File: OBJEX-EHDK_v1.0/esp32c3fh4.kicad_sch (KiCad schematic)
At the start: 34 parts

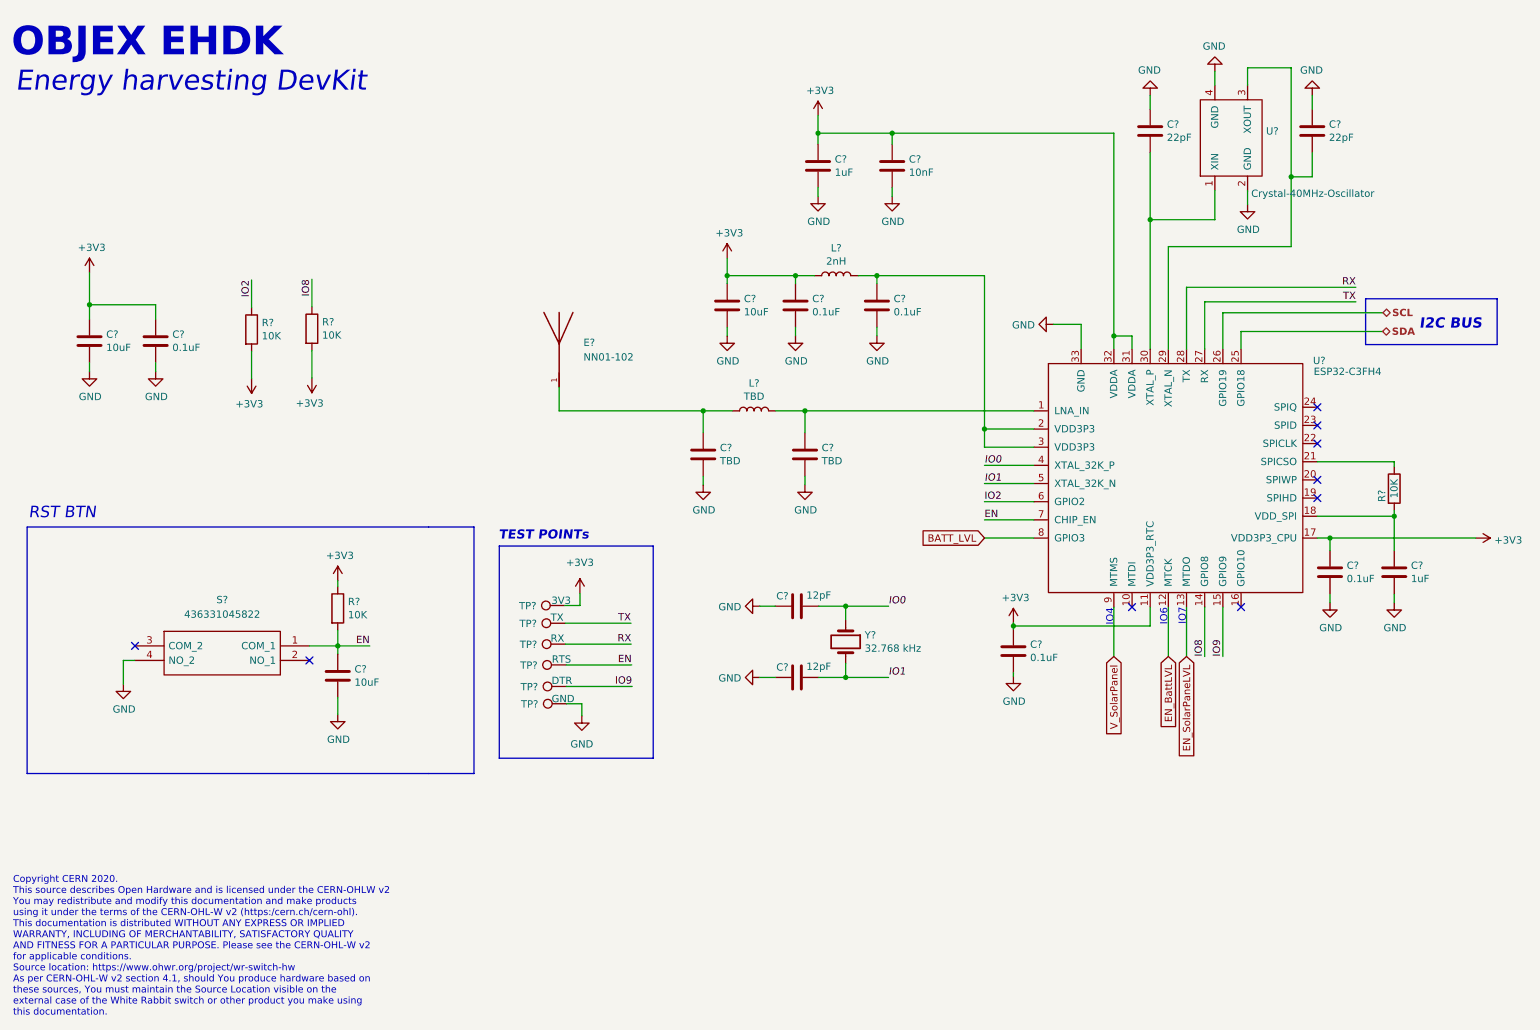
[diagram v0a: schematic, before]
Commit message: add: nRF52840 & SPV1050TTR
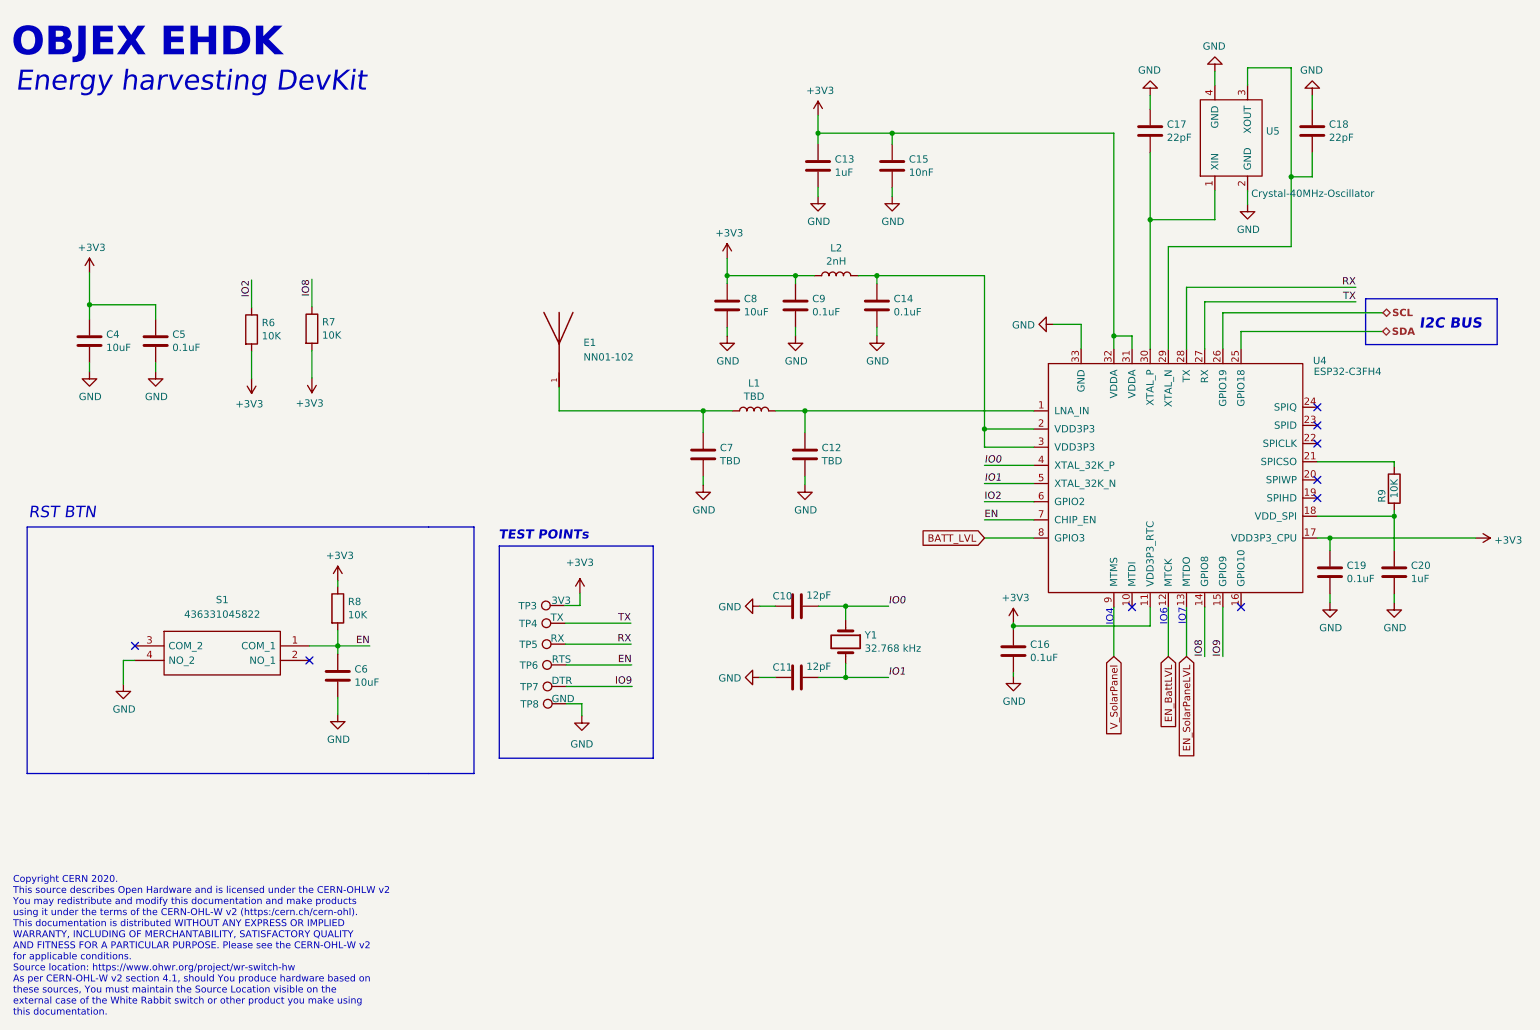
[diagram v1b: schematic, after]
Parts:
- gave numbers to parts that had none: 34

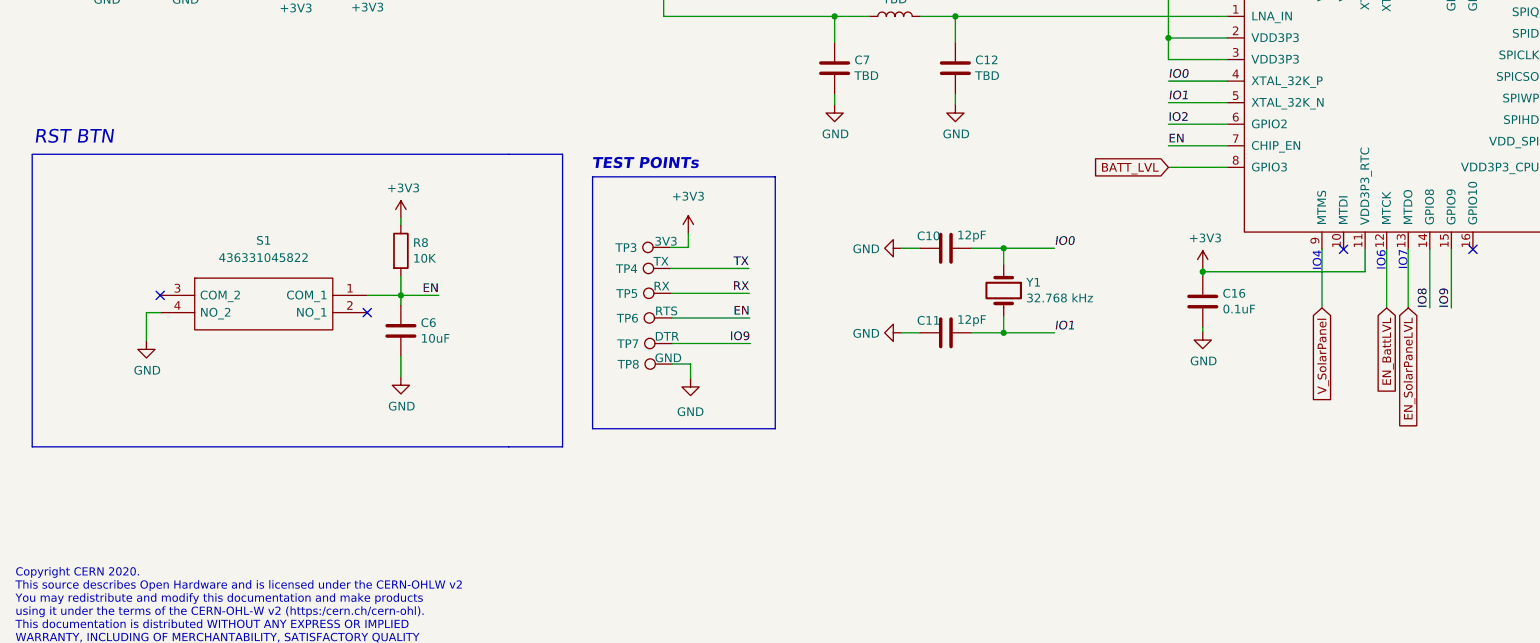
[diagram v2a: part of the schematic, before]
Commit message: Update design, EH ICs & Battery conn
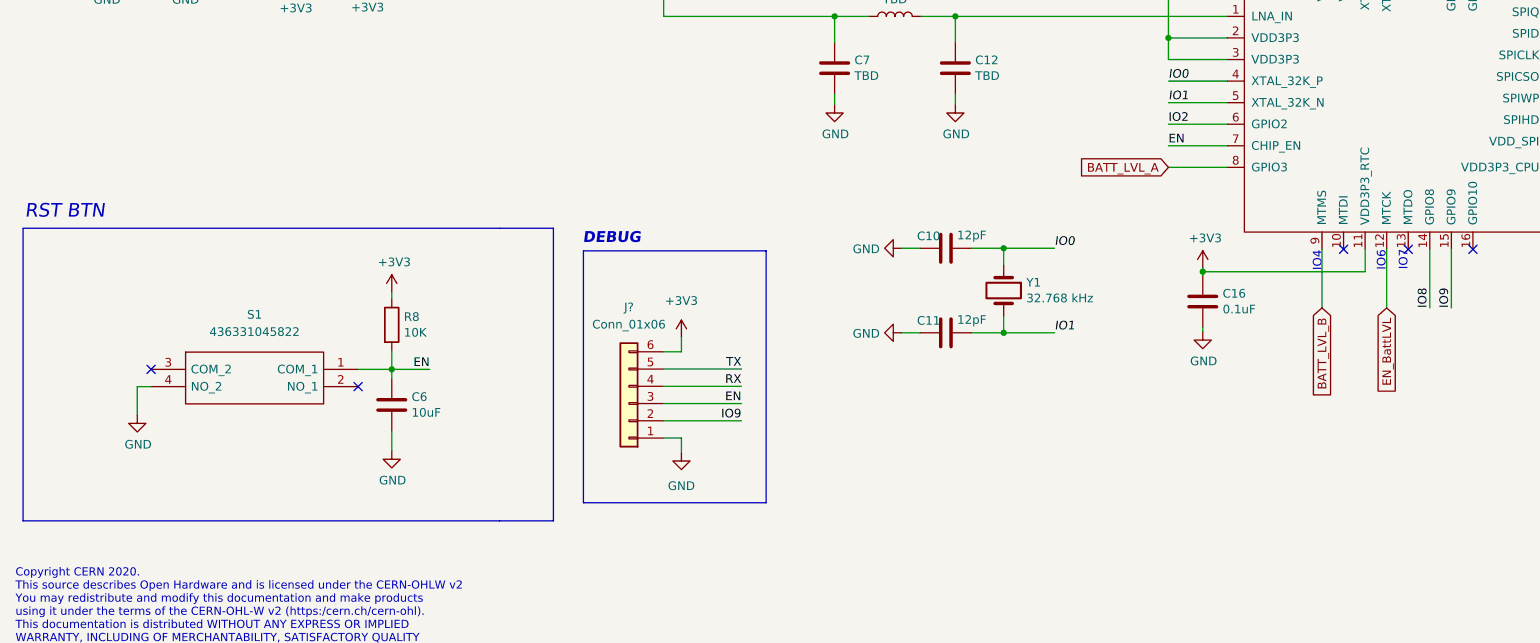
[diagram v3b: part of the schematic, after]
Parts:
- removed TP3: 3V3, TestPoint:TestPoint_Pad_D1.5mm, symbol Connector:TestPoint
- removed TP4: TX, TestPoint:TestPoint_Pad_D1.5mm, symbol Connector:TestPoint
- removed TP5: RX, TestPoint:TestPoint_Pad_D1.5mm, symbol Connector:TestPoint
- removed TP6: RTS, TestPoint:TestPoint_Pad_D1.5mm, symbol Connector:TestPoint
- removed TP7: DTR, TestPoint:TestPoint_Pad_D1.5mm, symbol Connector:TestPoint
- removed TP8: GND, TestPoint:TestPoint_Pad_D1.5mm, symbol Connector:TestPoint
- added J?: Conn_01x06, symbol Connector_Generic:Conn_01x06
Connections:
- net +3V3: now also J?.6 (Pin_6)
- net EN: now also J?.3 (Pin_3)
- net GND: now also J?.1 (Pin_1)
- net IO9: now also J?.2 (Pin_2)
- net RX: now also J?.4 (Pin_4)
- net TX: now also J?.5 (Pin_5)
- net BATT_LVL renamed BATT_LVL_A
- net EN_SolarPaneLVL: no longer names the net of U4.13 (MTDO)
- net V_SolarPanel renamed BATT_LVL_B
- no-connect marks 9 -> 10
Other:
- note added: "DEBUG"
- note removed: "TEST POINTs"
- moved on the sheet: C6, R8, S1
